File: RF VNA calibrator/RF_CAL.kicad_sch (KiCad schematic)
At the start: 7 parts

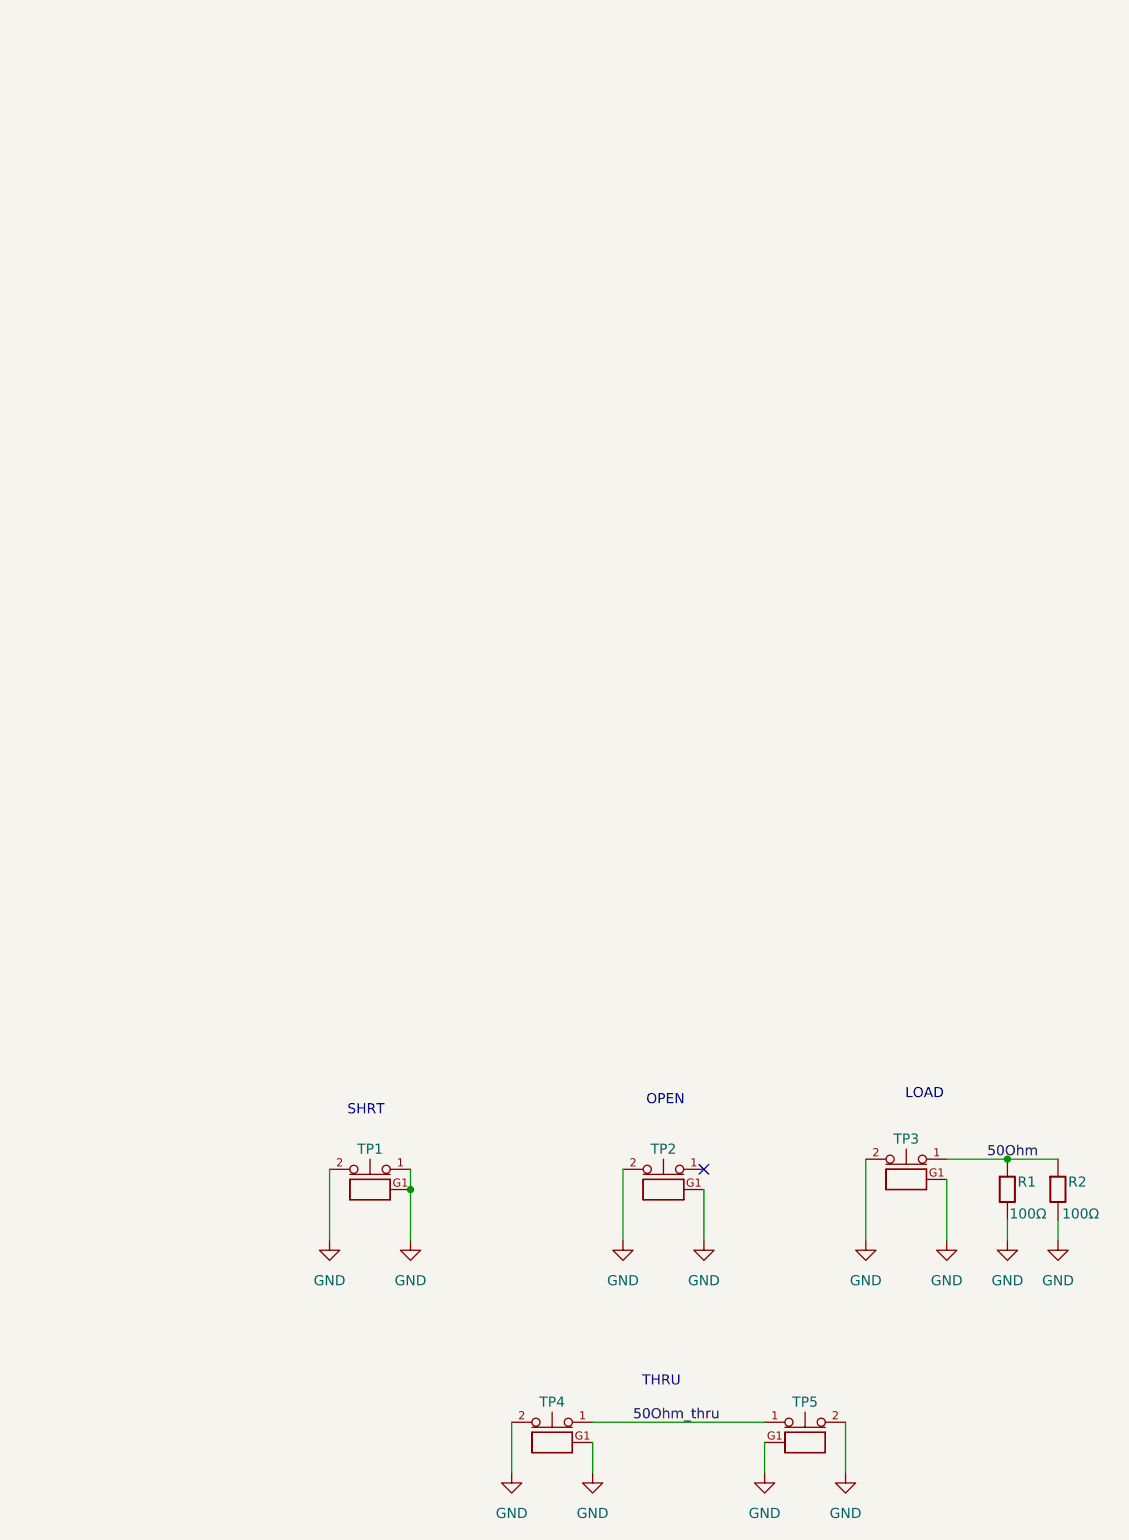
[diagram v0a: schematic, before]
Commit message: Cleanup & standardize schematic & PCB
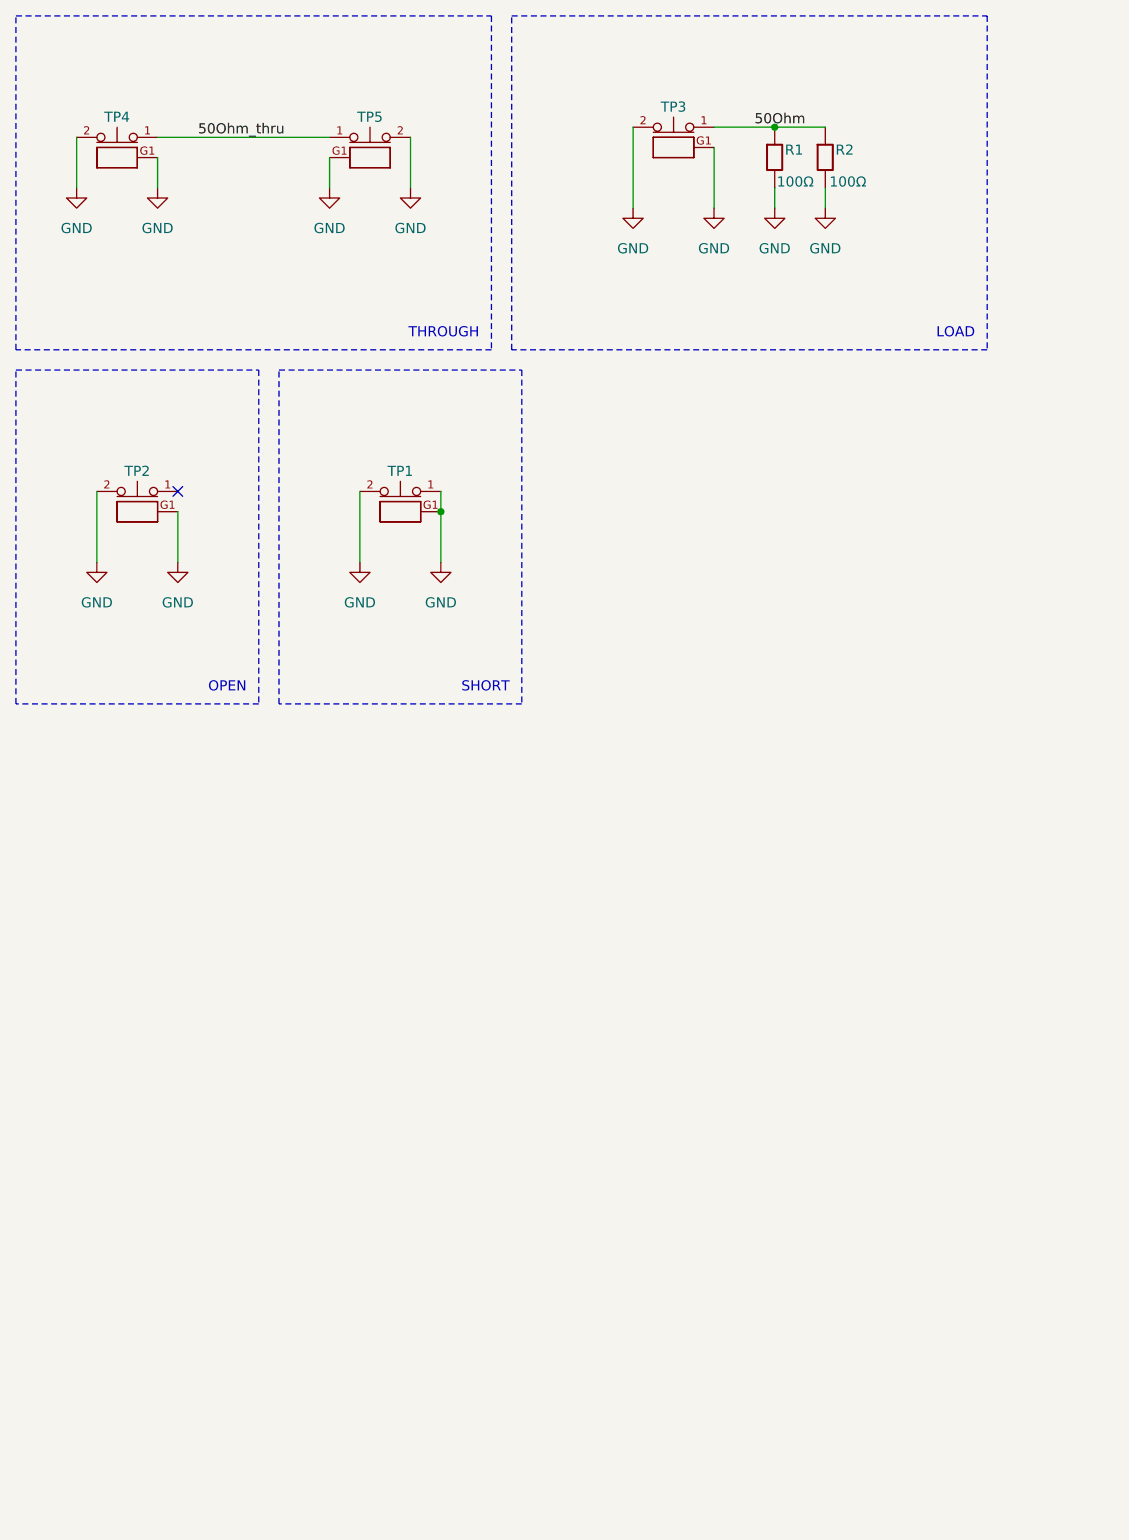
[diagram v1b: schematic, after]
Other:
- note added: "SHORT"
- note added: "THROUGH"
- note removed: "SHRT"
- note removed: "THRU"
- title: (none) -> VNA calibration board
- moved on the sheet: R1, R2, TP1, TP2, TP3, TP4, TP5

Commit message: Finish VNA calibration board, production files
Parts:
- R1, R2: MPN (none) -> RT0603FRD07100RL
- TP1, TP2, TP3, TP4, TP5: LCSC Part # MM8030-2610RK0 -> C91632
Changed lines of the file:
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@@
 			)
 		)
-		(property "LCSC Part #" "MM8030-2610RK0"
+		(property "LCSC Part #" "C91632"
 			(at 17.78 21.59 0)
 			(effects
@@
 			)
 		)
-		(property "LCSC Part #" "MM8030-2610RK0"
+		(property "LCSC Part #" "C91632"
 			(at 53.34 66.04 0)
 			(effects
@@
 			)
 		)
-		(property "LCSC Part #" "MM8030-2610RK0"
+		(property "LCSC Part #" "C91632"
 			(at 49.53 21.59 0)
 			(effects
@@
 			)
 		)
-		(property "LCSC Part #" "MM8030-2610RK0"
+		(property "LCSC Part #" "C91632"
 			(at 87.63 20.32 0)
 			(effects
@@
 			)
 		)
+		(property "MPN" "RT0603FRD07100RL"
+			(at 106.68 22.86 0)
+			(effects
+				(font
+					(size 1.27 1.27)
+				)
+				(hide yes)
+			)
+		)
 		(pin "2"
 		)
@@
 			)
 		)
-		(property "LCSC Part #" "MM8030-2610RK0"
+		(property "LCSC Part #" "C91632"
 			(at 20.32 66.04 0)
 			(effects
@@
 			(at 100.33 22.86 0)
 			(effects
+				(font
+					(size 1.27 1.27)
+				)
+				(hide yes)
+			)
+		)
+		(property "MPN" "RT0603FRD07100RL"
+			(at 100.33 22.86 0)
+			(effects
